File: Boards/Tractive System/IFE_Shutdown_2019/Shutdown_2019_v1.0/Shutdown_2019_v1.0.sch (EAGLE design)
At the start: 194 parts, among them Q1 DMN6140L-7, Q10 DMN6140L-7, Q11 DMP3099L-7, Q12 IRLML6346PBF, Q13 IRLML6346PBF, Q14 IRLML6346PBF, Q15 DMP3099L-7, Q16 DMN6140L-7, Q17 IRLML6346PBF, Q18 DMN6140L-7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

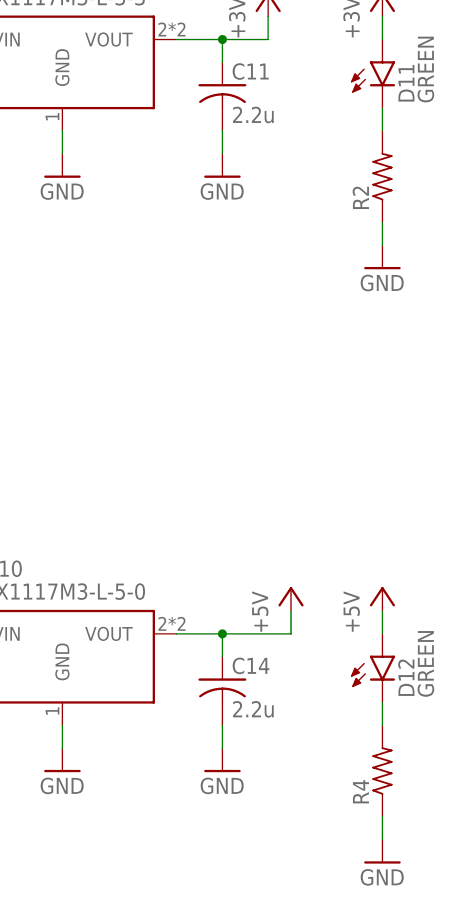
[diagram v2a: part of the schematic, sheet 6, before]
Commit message: fixing precharge + Shutdown
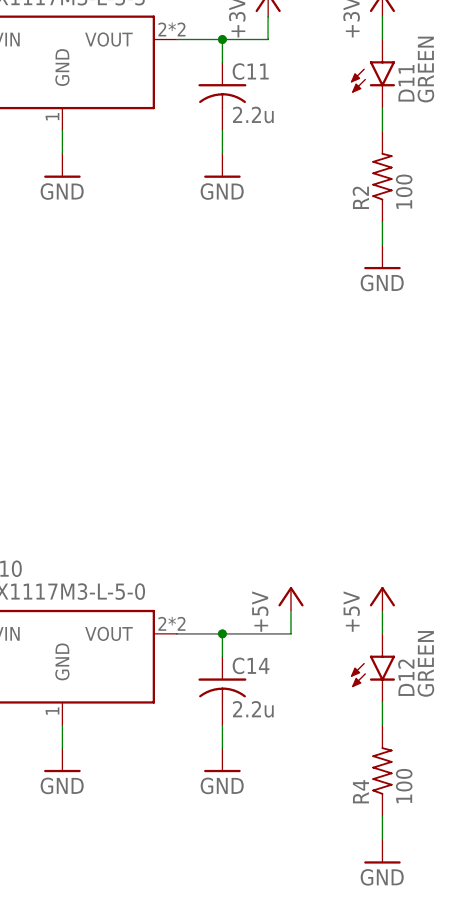
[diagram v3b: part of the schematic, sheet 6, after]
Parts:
- C21: value (none) -> 1u
- R2, R4: value (none) -> 100
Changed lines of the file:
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@@
 <part name="+3V17" library="supply1" library_urn="urn:adsk.eagle:library:371" deviceset="+3V3" device=""/>
 <part name="P+21" library="supply1" library_urn="urn:adsk.eagle:library:371" deviceset="+5V" device=""/>
-<part name="R4" library="rcl" library_urn="urn:adsk.eagle:library:334" deviceset="R-US_" device="R0603" package3d_urn="urn:adsk.eagle:package:23555/2"/>
-<part name="R2" library="rcl" library_urn="urn:adsk.eagle:library:334" deviceset="R-US_" device="R0603" package3d_urn="urn:adsk.eagle:package:23555/2"/>
+<part name="R4" library="rcl" library_urn="urn:adsk.eagle:library:334" deviceset="R-US_" device="R0603" package3d_urn="urn:adsk.eagle:package:23555/2" value="100"/>
+<part name="R2" library="rcl" library_urn="urn:adsk.eagle:library:334" deviceset="R-US_" device="R0603" package3d_urn="urn:adsk.eagle:package:23555/2" value="100"/>
 <part name="GND5" library="supply1" library_urn="urn:adsk.eagle:library:371" deviceset="GND" device=""/>
 <part name="GND6" library="supply1" library_urn="urn:adsk.eagle:library:371" deviceset="GND" device=""/>
@@
 <part name="U$18" library="STM" deviceset="LMV321L" device=""/>
 <part name="GND8" library="supply1" library_urn="urn:adsk.eagle:library:371" deviceset="GND" device=""/>
-<part name="C21" library="rcl" library_urn="urn:adsk.eagle:library:334" deviceset="C-US" device="C0603" package3d_urn="urn:adsk.eagle:package:23616/2"/>
+<part name="C21" library="rcl" library_urn="urn:adsk.eagle:library:334" deviceset="C-US" device="C0603" package3d_urn="urn:adsk.eagle:package:23616/2" value="1u"/>
 <part name="GND9" library="supply1" library_urn="urn:adsk.eagle:library:371" deviceset="GND" device=""/>
 <part name="P+22" library="supply1" library_urn="urn:adsk.eagle:library:371" deviceset="+5V" device=""/>
